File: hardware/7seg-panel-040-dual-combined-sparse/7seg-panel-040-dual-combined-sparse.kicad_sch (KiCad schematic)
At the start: 31 parts, among them J100 Conn_02x04_Odd_Even, J101 Conn_02x04_Odd_Even, J102 Conn_02x04_Odd_Even, J103 Conn_02x04_Odd_Even, J104 Conn_02x04_Odd_Even, J105 Conn_02x04_Odd_Even, U100 YH-2E20402-IK, U101 YH-2E20402-IK, U102 YH-2E20402-IK, U103 YH-2E20402-IK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

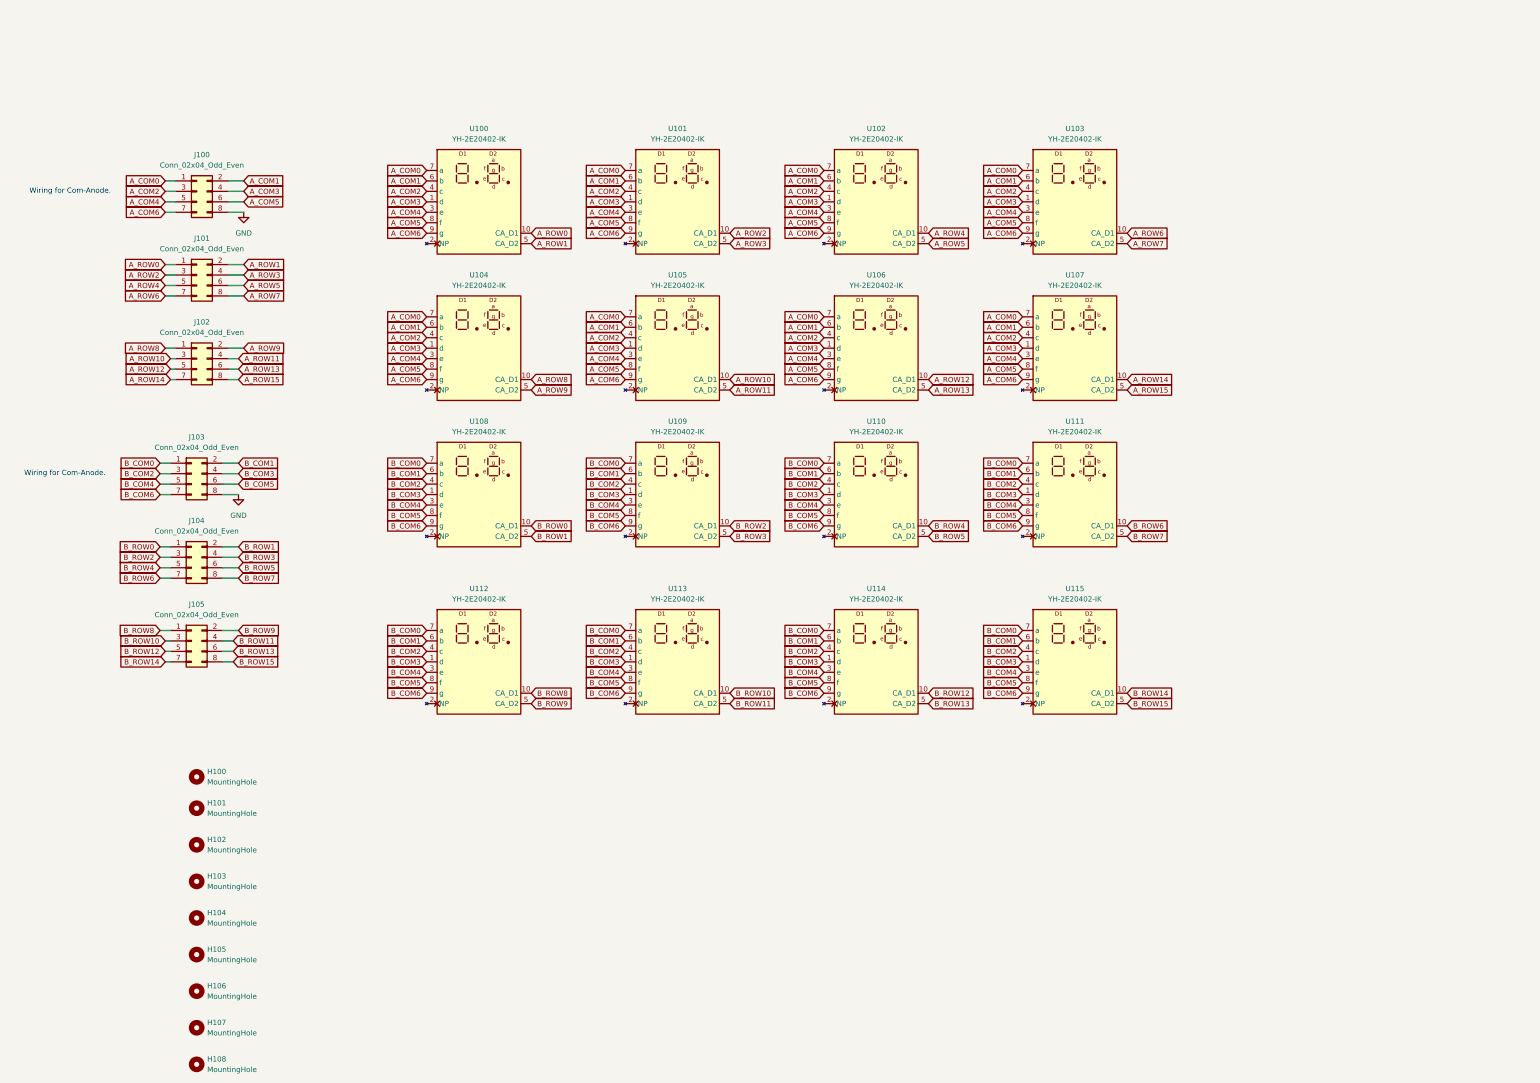
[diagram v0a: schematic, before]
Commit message: hardware: KiCad ファイルの更新と不要ファイルの削除
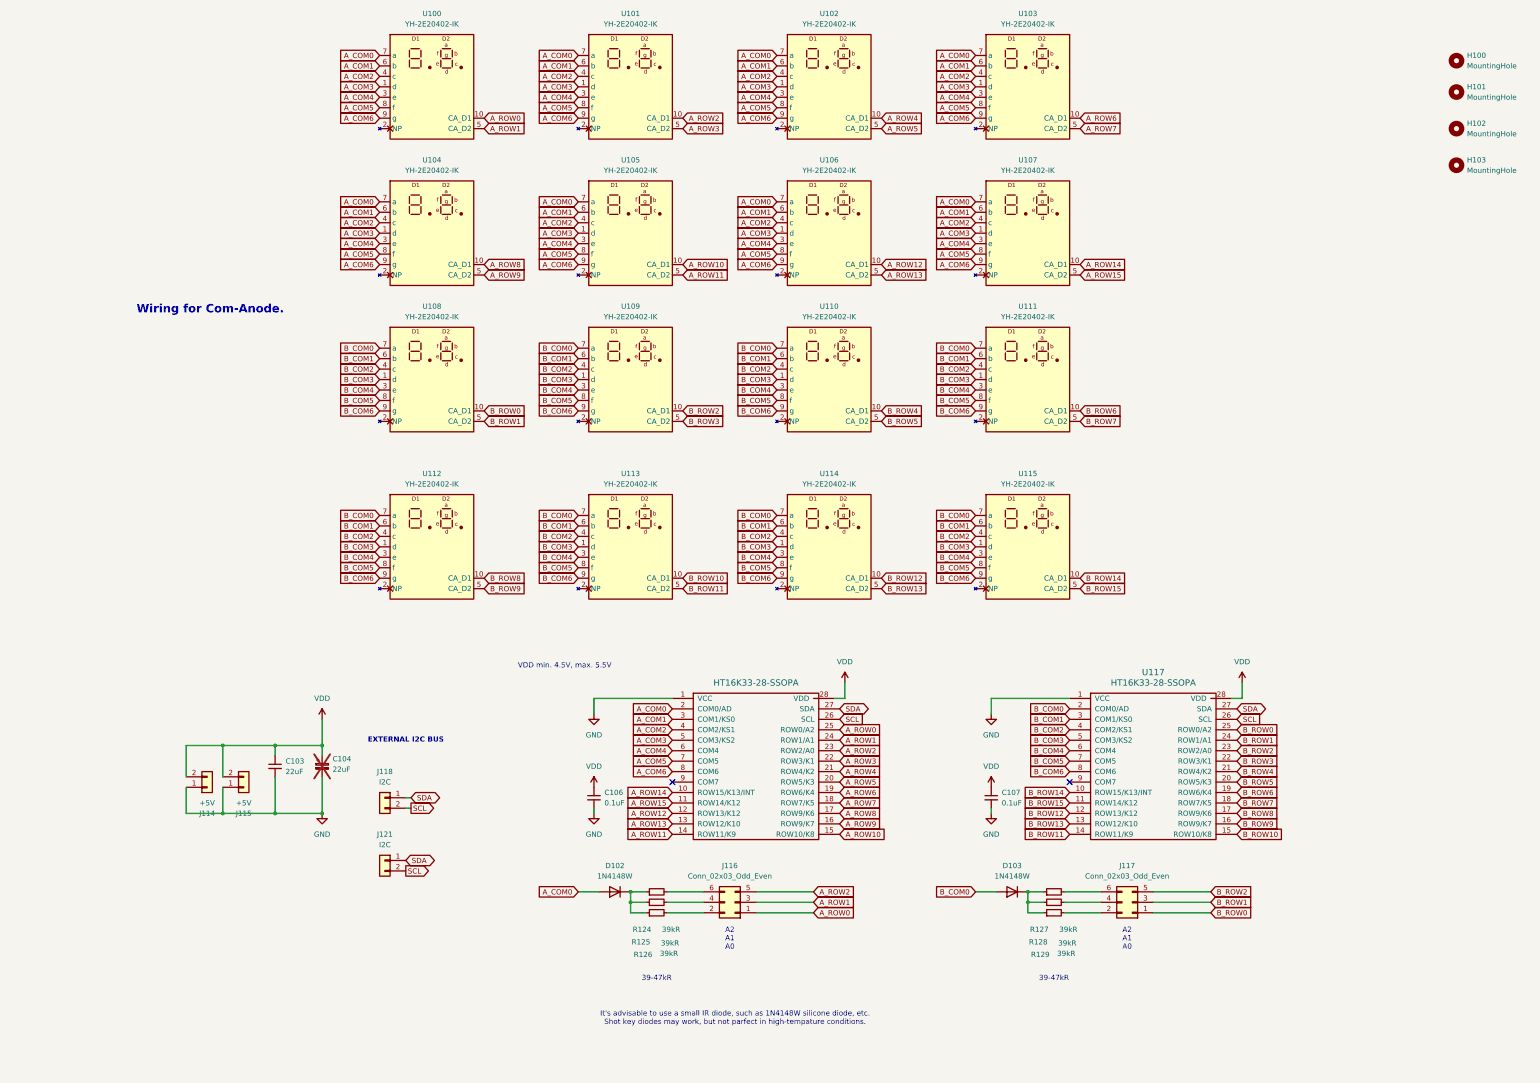
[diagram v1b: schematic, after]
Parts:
- removed H104, H105, H106, H107, H108: MountingHole, MountingHole:MountingHole_3.2mm_M3, symbol Mechanical:MountingHole
- removed J100, J101, J102, J103, J104, J105: Conn_02x04_Odd_Even, Connector_PinHeader_2.54mm:PinHeader_2x04_P2.54mm_Vertical, symbol Connector_Generic:Conn_02x04_Odd_Even
- added C103: 22uF, Capacitor_SMD:C_0603_1608Metric, symbol Device:C_Small
- added C104: 22uF, Capacitor_Tantalum_SMD:CP_EIA-3528-21_Kemet-B_HandSolder, symbol Device:C_Polarized_Small
- added C106, C107: 0.1uF, Capacitor_SMD:C_0603_1608Metric_Pad1.08x0.95mm_HandSolder, symbol Device:C_Small
- added D102, D103: 1N4148W, Diode_SMD:D_SOD-123, symbol Diode:1N4148W
- added J114, J115: +5V, Connector_JST:JST_XH_B2B-XH-AM_1x02_P2.50mm_Vertical, symbol Connector_Generic:Conn_01x02
- added J116, J117: Conn_02x03_Odd_Even, Connector_PinHeader_2.54mm:PinHeader_2x03_P2.54mm_Vertical, symbol Connector_Generic:Conn_02x03_Odd_Even
- added J118, J121: I2C, Connector_JST:JST_XH_B2B-XH-AM_1x02_P2.50mm_Vertical, symbol Connector_Generic:Conn_01x02
- added R124, R125, R126, R127, R128, R129: 39kR, Resistor_SMD:R_0603_1608Metric_Pad0.98x0.95mm_HandSolder, symbol Device:R_Small
- added U116, U117: HT16K33-28-SSOPA, Package_SO:SSOP-28_3.9x9.9mm_P0.635mm, symbol 7seg_led:HT16K33-28-SOPA
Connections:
- net A_COM0: now also D102.2 (A), U116.2 (COM0/AD)
- net A_COM1: now also U116.3 (COM1/KS0)
- net A_COM2: now also U116.4 (COM2/KS1)
- net A_COM3: now also U116.5 (COM3/KS2)
- net A_COM4: now also U116.6 (COM4)
- net A_COM5: now also U116.7 (COM5)
- net A_COM6: now also U116.8 (COM6)
- net A_ROW0: now also J116.1 (Pin_1), U116.25 (ROW0/A2)
- net A_ROW1: now also J116.3 (Pin_3), U116.24 (ROW1/A1)
- net A_ROW10: now also U116.15 (ROW10/K8)
- net A_ROW11: now also U116.14 (ROW11/K9)
- net A_ROW12: now also U116.12 (ROW13/K12)
- net A_ROW13: now also U116.13 (ROW12/K10)
- net A_ROW14: now also U116.10 (ROW15/K13/INT)
- net A_ROW15: now also U116.11 (ROW14/K12)
- net A_ROW2: now also J116.5 (Pin_5), U116.23 (ROW2/A0)
- net A_ROW3: now also U116.22 (ROW3/K1)
- net A_ROW4: now also U116.21 (ROW4/K2)
- net A_ROW5: now also U116.20 (ROW5/K3)
- net A_ROW6: now also U116.19 (ROW6/K4)
- net A_ROW7: now also U116.18 (ROW7/K5)
- net A_ROW8: now also U116.17 (ROW9/K6)
- net A_ROW9: now also U116.16 (ROW9/K7)
- net B_COM0: now also D103.2 (A), U117.2 (COM0/AD)
- net B_COM1: now also U117.3 (COM1/KS0)
- net B_COM2: now also U117.4 (COM2/KS1)
- net B_COM3: now also U117.5 (COM3/KS2)
- net B_COM4: now also U117.6 (COM4)
- net B_COM5: now also U117.7 (COM5)
- net B_COM6: now also U117.8 (COM6)
- net B_ROW0: now also J117.1 (Pin_1), U117.25 (ROW0/A2)
- net B_ROW1: now also J117.3 (Pin_3), U117.24 (ROW1/A1)
- net B_ROW10: now also U117.15 (ROW10/K8)
- net B_ROW11: now also U117.14 (ROW11/K9)
- net B_ROW12: now also U117.12 (ROW13/K12)
- net B_ROW13: now also U117.13 (ROW12/K10)
- net B_ROW14: now also U117.10 (ROW15/K13/INT)
- net B_ROW15: now also U117.11 (ROW14/K12)
- net B_ROW2: now also J117.5 (Pin_5), U117.23 (ROW2/A0)
- net B_ROW3: now also U117.22 (ROW3/K1)
- net B_ROW4: now also U117.21 (ROW4/K2)
- net B_ROW5: now also U117.20 (ROW5/K3)
- net B_ROW6: now also U117.19 (ROW6/K4)
- net B_ROW7: now also U117.18 (ROW7/K5)
- net B_ROW8: now also U117.17 (ROW9/K6)
- net B_ROW9: now also U117.16 (ROW9/K7)
- net GND: now also C103.2, C104.2, C106.2, C107.2, J114.1 (Pin_1), J115.1 (Pin_1), U116.1 (VCC), U117.1 (VCC)
- new net: D102.1 (K), R124.1, R125.1, R126.1
- new net: J116.4 (Pin_4), R125.2
- new net: J116.2 (Pin_2), R126.2
- new net: D103.1 (K), R127.1, R128.1, R129.1
- new net: J117.2 (Pin_2), R129.2
- new net: J117.4 (Pin_4), R128.2
- new net: J117.6 (Pin_6), R127.2
- new net: J116.6 (Pin_6), R124.2
- new net SCL: J118.2 (Pin_2), J121.2 (Pin_2), U116.26 (SCL), U117.26 (SCL)
- new net SDA: J118.1 (Pin_1), J121.1 (Pin_1), U116.27 (SDA), U117.27 (SDA)
- new net VDD: C103.1, C104.1, C106.1, C107.1, J114.2 (Pin_2), J115.2 (Pin_2), U116.28 (VDD), U117.28 (VDD)
- no-connect marks 0 -> 2
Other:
- note added: "39-47kR"
- note added: "A2 A1 A0"
- note added: "EXTERNAL I2C BUS"
- note added: "It's advisable to use a small IR diode, such as 1N4148W silicone diode, etc. Shot key diodes may work, but not parfect in high-tempature conditions."
- note added: "VDD min. 4.5V, max. 5.5V"
- moved on the sheet: H100, H101, H102, H103, U100, U101, U102, U103, U104, U105, U106, U107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
